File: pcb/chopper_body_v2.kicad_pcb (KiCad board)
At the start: 2 copper layers, 113.5 x 95.5 mm, 29 parts

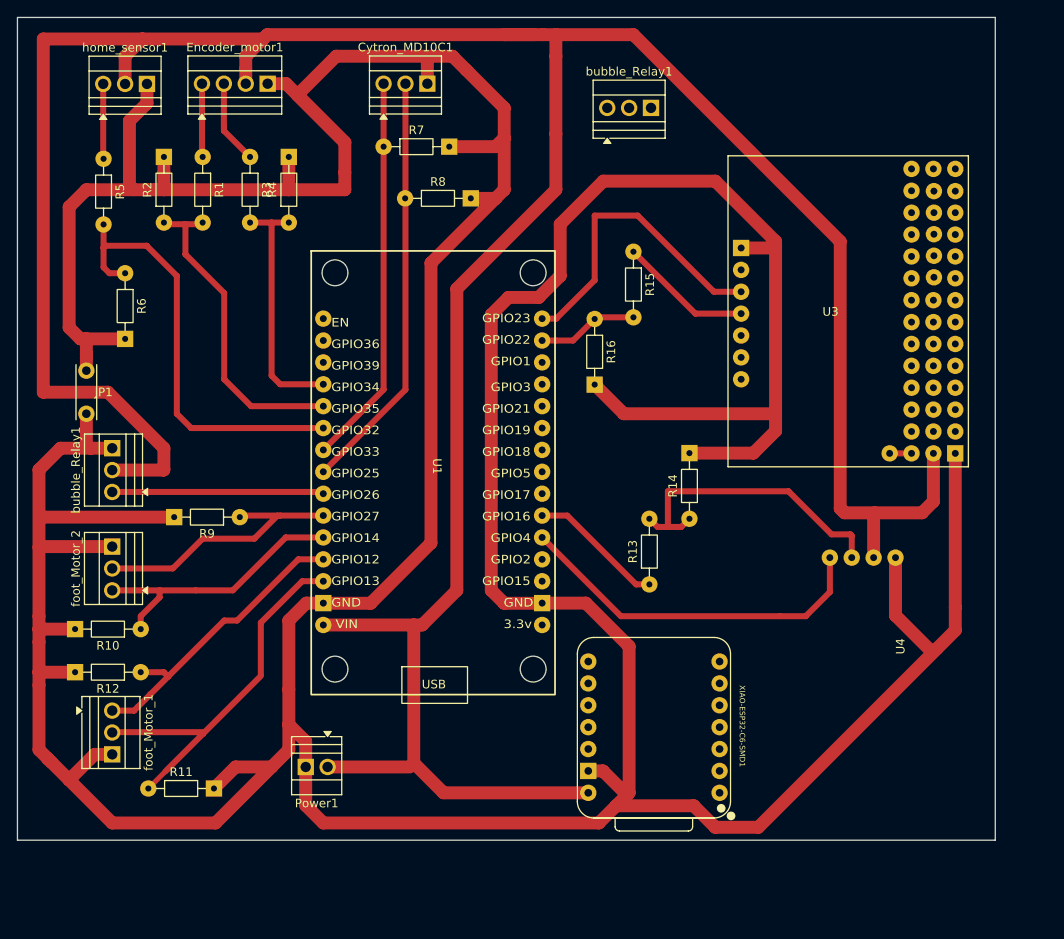
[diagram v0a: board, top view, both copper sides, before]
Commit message: Move drive motor pins off GPIO12/13, resync firmware pin map to PCB
Rerouted MDDS30 drive motors, dome I/O, Maestro, MP3, and bubbles relay
to new ESP32 pins on the PCB, primarily to get off GPIO12 (a boot-
strapping pin whose flash-voltage strap could cause reset loops if
pulled high during power-up). Updated config.h and the README pin
tables to match the new PCB copper.
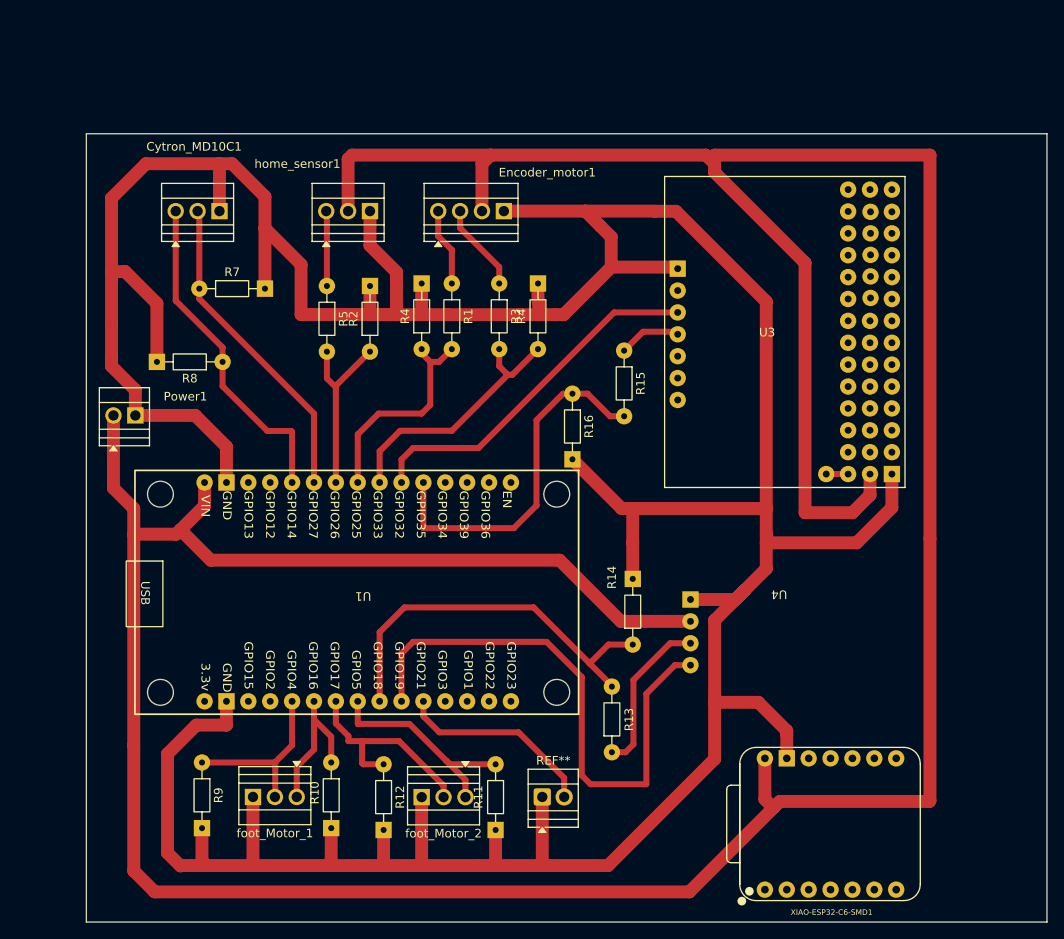
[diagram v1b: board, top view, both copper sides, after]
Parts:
- removed JP1: GND_BRIDGE, chopper_library:GND_Wire_Jumper
- removed the R4 at (56.0, 42.8)
- removed R6: 20K, Resistor_THT:R_Axial_DIN0204_L3.6mm_D1.6mm_P7.62mm_Horizontal
- removed bubble_Relay1 (x2): Signal_5v_GND, TerminalBlock:TerminalBlock_Xinya_XY308-2.54-3P_1x03_P2.54mm_Horizontal
- added R4: 20K, Resistor_THT:R_Axial_DIN0204_L3.6mm_D1.6mm_P7.62mm_Horizontal, F.Cu at (84.9, 57.5)
- added R4: 20K, Resistor_THT:R_Axial_DIN0204_L3.6mm_D1.6mm_P7.62mm_Horizontal, F.Cu at (71.4, 57.5)
- added REF**: Relay, TerminalBlock:TerminalBlock_Xinya_XY308-2.54-2P_1x02_P2.54mm_Horizontal, F.Cu at (85.4, 109.5)
- foot_Motor_1: value IN2_AN2_GND -> IN1_IN2_GND
- moved Power1 47.8 mm to (35.6, 65.2), turned to 0 degrees
- moved foot_Motor_2 47.5 mm to (76.5, 109.5), turned to 180 degrees
- moved R11 40.4 mm to (80.0, 105.7), turned to -90 degrees
- moved R1 32.4 mm to (74.9, 49.9)
- moved R3 32.4 mm to (80.4, 49.9)
- moved Encoder_motor1 31.2 mm to (73.3, 41.5)
- moved R12 30.1 mm to (67.0, 105.7), turned to -90 degrees
- moved R5 29.8 mm to (60.4, 50.2)
- moved home_sensor1 29.8 mm to (60.3, 41.5)
- moved R9 28.8 mm to (45.9, 105.5), turned to -90 degrees
- moved R8 28.4 mm to (48.3, 59.0), turned to 180 degrees
- moved Cytron_MD10C1 28.3 mm to (42.9, 41.5)
- moved R2 28.2 mm to (65.4, 57.8)
- moved R7 27.0 mm to (45.6, 50.5)
- moved R10 27.0 mm to (60.9, 105.5), turned to -90 degrees
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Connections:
- net Net-(Encoder_motor1-Pin_1) renamed encoder_a_signal
- net Net-(Encoder_motor1-Pin_2) renamed encoder_b_signal
- net Net-(R15-Pad1) renamed pololu_tx
- net Net-(U3-PadVSRV) renamed vin_pololu
- net Net-(home_sensor1-Pin_1) renamed home_sensor_signal
- Cytron_MD10C1 pad 1: Net-(Cytron_MD10C1-Pin_1) -> MD10_DIR
- Cytron_MD10C1 pad 2: Net-(Cytron_MD10C1-Pin_2) -> MD10PWM
- R1 pad 2: Net-(U1-GPIO35) -> encoder_a_resistor
- R10 pad 1: Net-(U1-GPIO14) -> IN2
- R11 pad 1: Net-(U1-GPIO13) -> AN2
- R12 pad 1: Net-(U1-GPIO12) -> AN1
- R13 pad 1: /audio_tx_board -> audio_tx
- R13 pad 2: Net-(U1-GPIO16) -> audio_tx_resistor
- R14 pad 1: Net-(U1-GPIO16) -> audio_tx_resistor
- R2 pad 1: Net-(U1-GPIO35) -> home_sensor_resistant
- R3 pad 2: Net-(U1-GPIO34) -> encoder_b_resistor
- R5 pad 2: Net-(U1-GPIO32) -> home_sensor_resistant
- R7 pad 1: Net-(Cytron_MD10C1-Pin_1) -> MD10PWM
- R8 pad 1: Net-(Cytron_MD10C1-Pin_2) -> MD10_DIR
- R9 pad 1: unconnected-(U1-GPIO3-Pad27) -> IN1
- U1 pad 10: Net-(U1-GPIO32) -> pololu_rx
- U1 pad 11: Net-(U1-GPIO35) -> pololu_tx_resistor
- U1 pad 12: Net-(U1-GPIO34) -> (no net)
- U1 pad 13: unconnected-(U1-GPIO39-Pad13) -> (no net)
- U1 pad 14: unconnected-(U1-GPIO36-Pad14) -> (no net)
- U1 pad 15: unconnected-(U1-EN-Pad15) -> (no net)
- U1 pad 16: 3.3v -> (no net)
- U1 pad 20: audio_rx -> IN1
- U1 pad 21: /audio_tx_board -> IN2
- U1 pad 22: Gpio17 -> AN1
- U1 pad 23: Net-(U1-GPIO5) -> AN2
- U1 pad 24: unconnected-(U1-GPIO18-Pad24) -> audio_tx_resistor
- U1 pad 25: unconnected-(U1-GPIO19-Pad25) -> audio_rx
- U1 pad 26: unconnected-(U1-GPIO21-Pad26) -> relay_signal
- U1 pad 27: unconnected-(U1-3.3v-Pad16) -> (no net)
- U1 pad 28: unconnected-(U1-GPIO1-Pad28) -> (no net)
- U1 pad 29: pololu_tx_resistor -> (no net)
- U1 pad 3: Net-(U1-GPIO13) -> (no net)
- U1 pad 30: /pololu_rx -> (no net)
- U1 pad 4: Net-(U1-GPIO12) -> (no net)
- U1 pad 5: Net-(U1-GPIO14) -> MD10_DIR
- U1 pad 6: unconnected-(U1-GPIO3-Pad27) -> MD10PWM
- U1 pad 7: Net-(U1-GPIO26) -> home_sensor_resistant
- U1 pad 8: Net-(Cytron_MD10C1-Pin_2) -> encoder_a_resistor
- U1 pad 9: Net-(Cytron_MD10C1-Pin_1) -> encoder_b_resistor
- U3 pad 0: unconnected-(U3-Pad0) -> (no net)
- U3 pad 1: unconnected-(U3-Pad1) -> (no net)
- U3 pad 10: unconnected-(U3-Pad10) -> (no net)
- U3 pad 11: unconnected-(U3-Pad11) -> (no net)
- U3 pad 2: unconnected-(U3-Pad2) -> (no net)
- U3 pad 3: unconnected-(U3-Pad3) -> (no net)
- U3 pad 4: unconnected-(U3-Pad4) -> (no net)
- U3 pad 5: unconnected-(U3-Pad5) -> (no net)
- U3 pad 5V: unconnected-(U3-Pad5V) -> (no net)
- U3 pad 6: unconnected-(U3-Pad6) -> (no net)
- U3 pad 7: unconnected-(U3-Pad7) -> (no net)
- U3 pad 8: unconnected-(U3-Pad8) -> (no net)
- U3 pad 9: unconnected-(U3-Pad9) -> (no net)
- U3 pad ERR: unconnected-(U3-PadERR) -> (no net)
- U3 pad GND0: unconnected-(U3-PadGND0) -> (no net)
- U3 pad GND1: unconnected-(U3-PadGND1) -> (no net)
- U3 pad GND10: unconnected-(U3-PadGND10) -> (no net)
- U3 pad GND11: unconnected-(U3-PadGND11) -> (no net)
- U3 pad GND2: unconnected-(U3-PadGND2) -> (no net)
- U3 pad GND3: unconnected-(U3-PadGND3) -> (no net)
- U3 pad GND4: unconnected-(U3-PadGND4) -> (no net)
- U3 pad GND5: unconnected-(U3-PadGND5) -> (no net)
- U3 pad GND5V: unconnected-(U3-PadGND5V) -> (no net)
- U3 pad GND6: unconnected-(U3-PadGND6) -> (no net)
- U3 pad GND7: unconnected-(U3-PadGND7) -> (no net)
- U3 pad GND8: unconnected-(U3-PadGND8) -> (no net)
- U3 pad GND9: unconnected-(U3-PadGND9) -> (no net)
- U3 pad RST: unconnected-(U3-PadRST) -> (no net)
- U3 pad Rx: /pololu_rx -> pololu_rx
- U3 pad TXIn: unconnected-(U3-PadTXIn) -> (no net)
- U3 pad V0: unconnected-(U3-PadV0) -> (no net)
- U3 pad V1: unconnected-(U3-PadV1) -> (no net)
- U3 pad V10: unconnected-(U3-PadV10) -> (no net)
- U3 pad V11: unconnected-(U3-PadV11) -> (no net)
- U3 pad V2: unconnected-(U3-PadV2) -> (no net)
- U3 pad V3: unconnected-(U3-PadV3) -> (no net)
- U3 pad V4: unconnected-(U3-PadV4) -> (no net)
- U3 pad V5: unconnected-(U3-PadV5) -> (no net)
- U3 pad V5V: unconnected-(U3-PadV5V) -> (no net)
- U3 pad V6: unconnected-(U3-PadV6) -> (no net)
- U3 pad V7: unconnected-(U3-PadV7) -> (no net)
- U3 pad V8: unconnected-(U3-PadV8) -> (no net)
- U3 pad V9: unconnected-(U3-PadV9) -> (no net)
- U3 pad VinBoard: unconnected-(U3-PadVinBoard) -> (no net)
- U4 pad RX: Net-(U1-GPIO16) -> audio_rx
- XIAO-ESP32-C6-SMD1 pad 1: unconnected-(XIAO-ESP32-C6-SMD1-D0-Pad1) -> (no net)
- XIAO-ESP32-C6-SMD1 pad 10: unconnected-(XIAO-ESP32-C6-SMD1-D9-Pad10) -> (no net)
- XIAO-ESP32-C6-SMD1 pad 11: unconnected-(XIAO-ESP32-C6-SMD1-D10-Pad11) -> (no net)
- XIAO-ESP32-C6-SMD1 pad 12: unconnected-(XIAO-ESP32-C6-SMD1-3V3_OUT-Pad12) -> (no net)
- XIAO-ESP32-C6-SMD1 pad 2: unconnected-(XIAO-ESP32-C6-SMD1-D1-Pad2) -> (no net)
- XIAO-ESP32-C6-SMD1 pad 3: unconnected-(XIAO-ESP32-C6-SMD1-D2-Pad3) -> (no net)
- XIAO-ESP32-C6-SMD1 pad 4: unconnected-(XIAO-ESP32-C6-SMD1-D3-Pad4) -> (no net)
- XIAO-ESP32-C6-SMD1 pad 5: unconnected-(XIAO-ESP32-C6-SMD1-D4-Pad5) -> (no net)
- XIAO-ESP32-C6-SMD1 pad 6: unconnected-(XIAO-ESP32-C6-SMD1-D5-Pad6) -> (no net)
- XIAO-ESP32-C6-SMD1 pad 7: unconnected-(XIAO-ESP32-C6-SMD1-D6-Pad7) -> (no net)
- XIAO-ESP32-C6-SMD1 pad 8: unconnected-(XIAO-ESP32-C6-SMD1-D7-Pad8) -> (no net)
- XIAO-ESP32-C6-SMD1 pad 9: unconnected-(XIAO-ESP32-C6-SMD1-D8-Pad9) -> (no net)
- foot_Motor_1 pad 1: Net-(U1-GPIO12) -> IN2
- foot_Motor_1 pad 2: Net-(U1-GPIO13) -> IN1
- foot_Motor_2 pad 1: Net-(U1-GPIO14) -> AN2
- foot_Motor_2 pad 2: unconnected-(U1-GPIO3-Pad27) -> AN1
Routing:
- net GND: track 676.0 -> 483.0 mm
- net +5V: track 372.2 -> 446.4 mm
- net Net-(U1-GPIO32): track 51.5 -> 0.00 mm
- net Net-(Cytron_MD10C1-Pin_2): track 49.0 -> 0.00 mm
- net audio_tx_resistor: track 0.00 -> 46.0 mm
- net Net-(Cytron_MD10C1-Pin_1): track 45.4 -> 0.00 mm
- net Net-(U1-GPIO13): track 44.4 -> 0.00 mm
- net pololu_rx: track 0.00 -> 41.8 mm
- net MD10_DIR: track 0.00 -> 38.7 mm
- net Net-(U1-GPIO35): track 37.2 -> 0.00 mm
- net MD10PWM: track 0.00 -> 37.1 mm
- net /pololu_rx: track 36.1 -> 0.00 mm
- net Net-(U1-GPIO12): track 36.0 -> 0.00 mm
- net Net-(U1-GPIO16): track 35.6 -> 0.00 mm
- net Net-(U1-GPIO14): track 32.5 -> 0.00 mm
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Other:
- board size 113.5 x 95.5 mm -> 111.5 x 91.5 mm
- board text added: "R8"
